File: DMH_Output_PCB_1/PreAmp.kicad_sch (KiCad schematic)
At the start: 0 parts

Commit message: Designed preamp circuit
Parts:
- added C15, C18, C20, C22: 100pF, Capacitor_THT:C_Disc_D3.0mm_W2.0mm_P2.50mm, symbol Device:C
- added C16, C17, C19, C21: 47uF, Capacitor_THT:C_Disc_D4.3mm_W1.9mm_P5.00mm, symbol Device:C
- added R60, R63, R73, R81: 100R, Resistor_THT:R_Axial_DIN0207_L6.3mm_D2.5mm_P7.62mm_Horizontal, symbol Device:R_US
- added R61, R62, R64, R65, R75, R76, R82, R83: 100k, Resistor_THT:R_Axial_DIN0207_L6.3mm_D2.5mm_P7.62mm_Horizontal, symbol Device:R_US
- added R66, R67, R68, R69, R72, R77, R78, R79: 470R, Resistor_THT:R_Axial_DIN0207_L6.3mm_D2.5mm_P7.62mm_Horizontal, symbol Device:R_US
- added R70, R71, R74, R80: 1k, Resistor_THT:R_Axial_DIN0207_L6.3mm_D2.5mm_P7.62mm_Horizontal, symbol Device:R_US
- added RV3: B10k_Dual, Potentiometer_THT:Potentiometer_Alpha_RD902F-40-00D_Dual_Vertical, symbol Device:R_Potentiometer_Dual_Separate
- added U16, U17, U18, U19: NE5532, symbol Amplifier_Operational:NE5532
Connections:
- new net: C17.2, R65.2, U16.3 (+)
- new net: C21.2, R83.2, U18.5 (+)
- new net: R66.1, U16.1, U16.2 (-)
- new net: R72.1, R74.1, R77.2, U19.2 (-)
- new net: R78.2, R79.2, R80.2, U19.3 (+)
- new net: C21.1, C22.2, R81.2, R82.2
- new net: RV3.2, U17.5 (+)
- new net: C19.1, C20.2, R73.2, R75.2
- new net: R67.1, U16.6 (-), U16.7
- new net: R67.2, R69.2, R70.2, U17.3 (+)
- new net: C15.2, C16.1, R60.2, R61.2
- new net: C17.1, C18.2, R63.2, R64.2
- new net: C19.2, R76.2, U18.3 (+)
- new net: R66.2, R68.1, R71.1, U17.2 (-)
- new net: R68.2, U17.6 (-), U17.7
- new net: C16.2, R62.2, U16.5 (+)
- new net: R77.1, U18.1, U18.2 (-)
- new net: RV3.5, U19.5 (+)
- new net: R72.2, U19.6 (-), U19.7
- new net: R78.1, U18.6 (-), U18.7
- new net GND: C15.1, C18.1, C20.1, C22.1, R61.1, R62.1, R64.1, R65.1, R69.1, R70.1, R75.1, R76.1, R79.1, R80.1, R82.1, R83.1, RV3.1, RV3.4
- new net L_Euro_OUT: R71.2, RV3.3, U17.1
- new net L_Ext_IN+: R60.1
- new net L_Ext_IN-: R63.1
- new net R_Euro_OUT: R74.2, RV3.6, U19.1
- new net R_Ext_IN+: R81.1
- new net R_Ext_IN-: R73.1

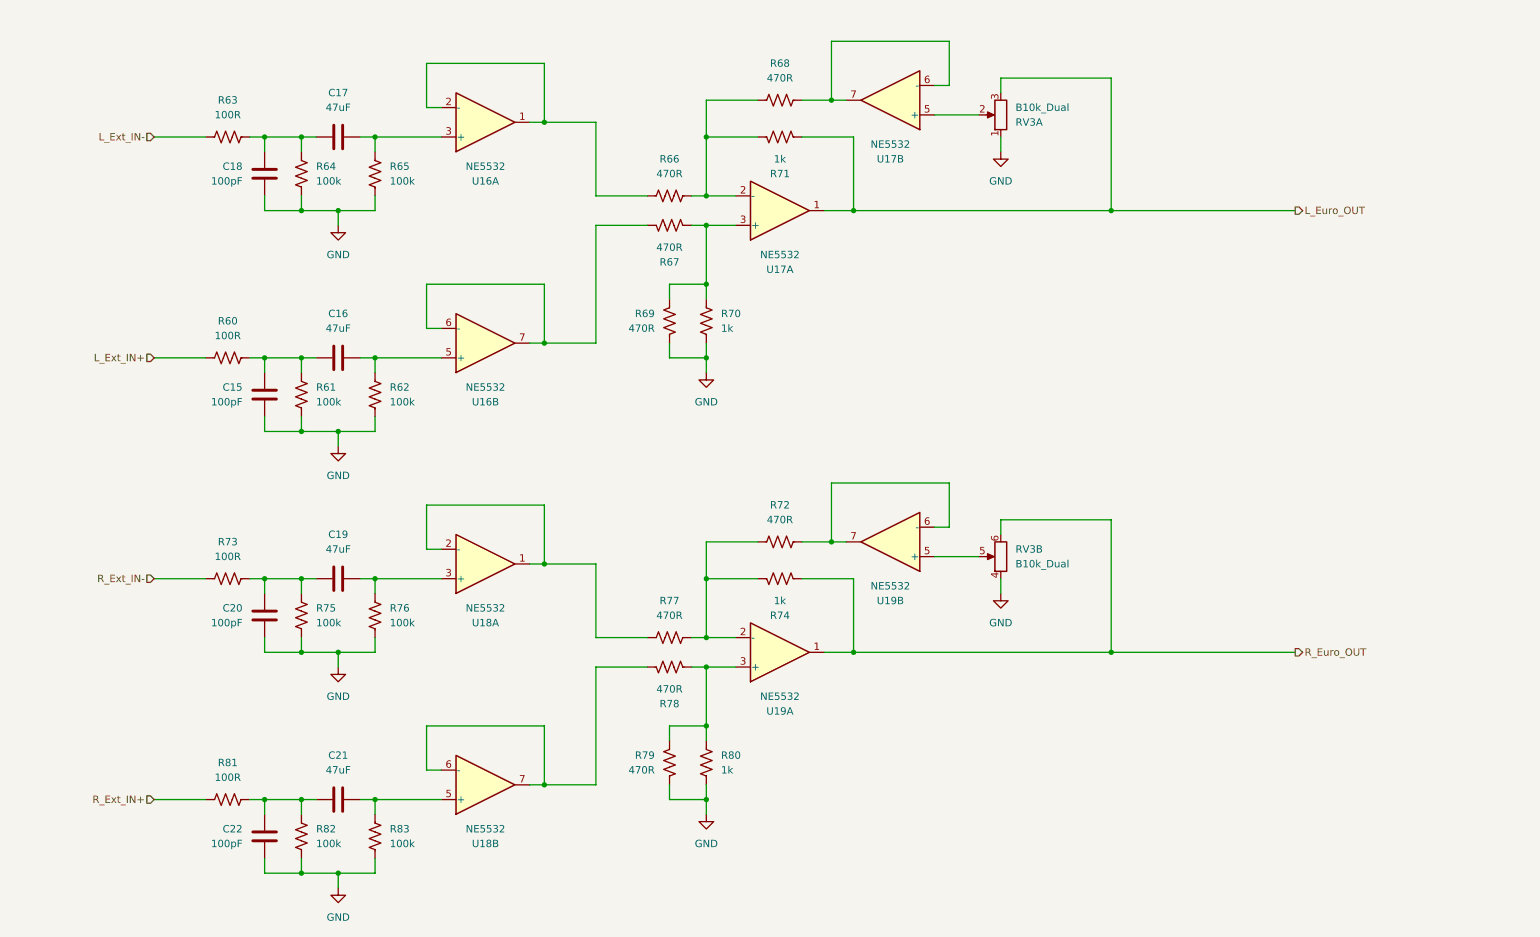
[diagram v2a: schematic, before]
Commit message: Redesigned external input preamp
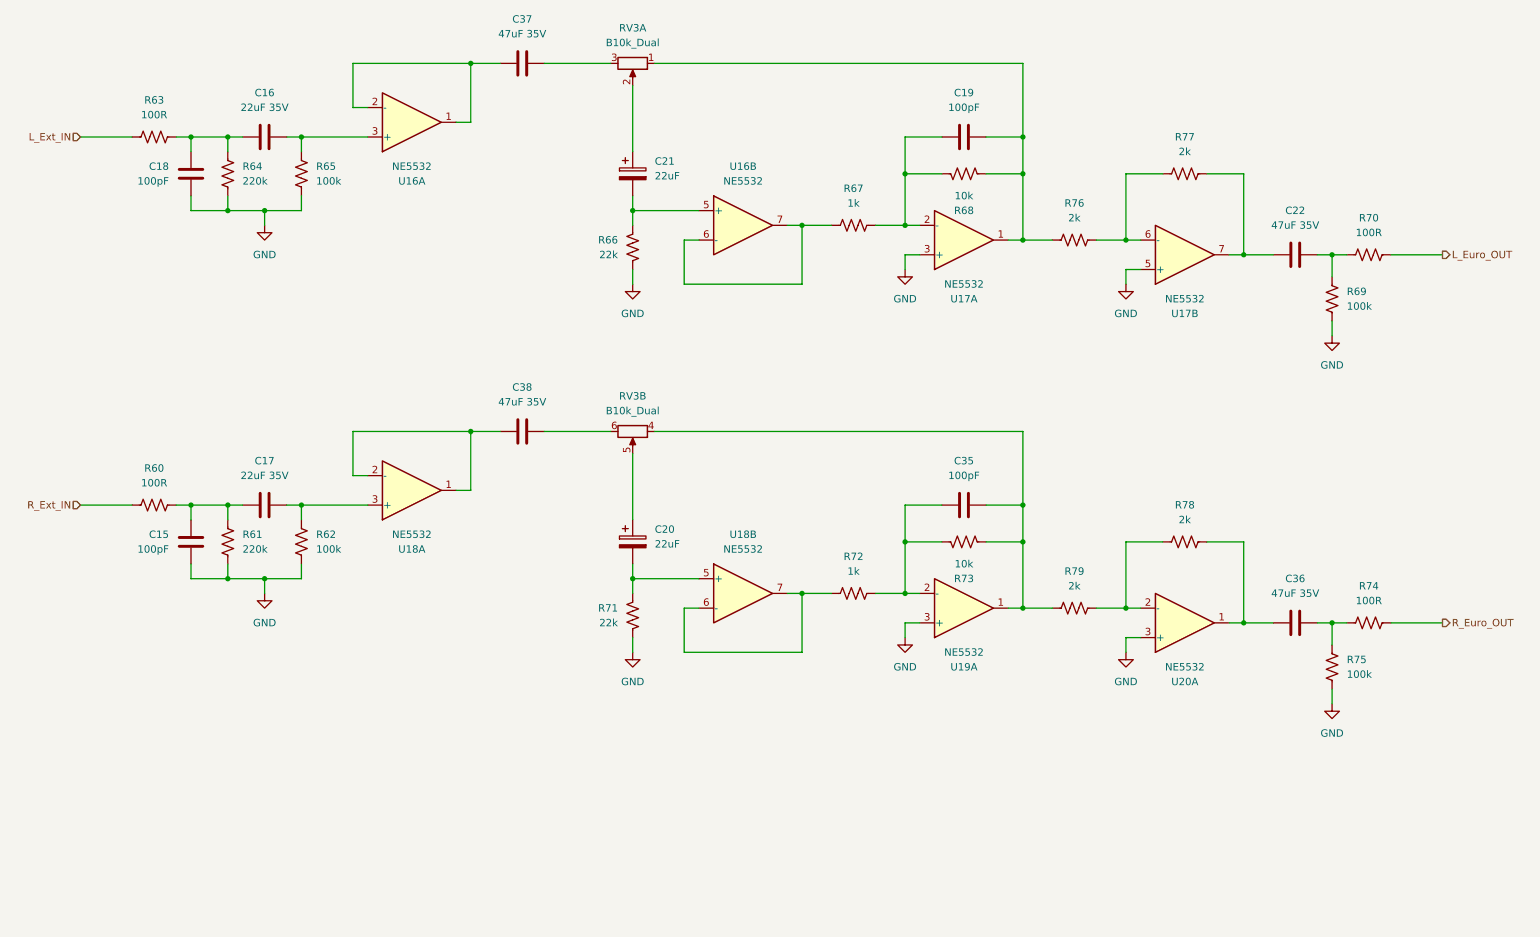
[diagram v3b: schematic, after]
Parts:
- removed C20: 100pF, Capacitor_THT:C_Disc_D3.0mm_W2.0mm_P2.50mm, symbol Device:C
- removed C21: 47uF, Capacitor_THT:C_Disc_D4.3mm_W1.9mm_P5.00mm, symbol Device:C
- removed R80: 1k, Resistor_THT:R_Axial_DIN0207_L6.3mm_D2.5mm_P7.62mm_Horizontal, symbol Device:R_US
- removed R81: 100R, Resistor_THT:R_Axial_DIN0207_L6.3mm_D2.5mm_P7.62mm_Horizontal, symbol Device:R_US
- removed R82, R83: 100k, Resistor_THT:R_Axial_DIN0207_L6.3mm_D2.5mm_P7.62mm_Horizontal, symbol Device:R_US
- removed unit 2 of U19
- added C20, C21: 22uF, Capacitor_THT:CP_Radial_D5.0mm_P2.00mm, symbol Device:C_Polarized
- added C35: 100pF, Capacitor_THT:C_Disc_D3.0mm_W2.0mm_P2.50mm, symbol Device:C
- added C36, C37, C38: 47uF 35V, Capacitor_THT:C_Radial_D8.0mm_H11.5mm_P3.50mm, symbol Device:C
- added U20: NE5532, symbol Amplifier_Operational:NE5532
- C16, C17: value 47uF -> 22uF 35V; footprint Capacitor_THT:C_Disc_D4.3mm_W1.9mm_P5.00mm -> Capacitor_THT:C_Radial_D8.0mm_H11.5mm_P3.50mm
- C19: value 47uF -> 100pF; footprint Capacitor_THT:C_Disc_D4.3mm_W1.9mm_P5.00mm -> Capacitor_THT:C_Disc_D3.0mm_W2.0mm_P2.50mm
- C22: value 100pF -> 47uF 35V; footprint Capacitor_THT:C_Disc_D3.0mm_W2.0mm_P2.50mm -> Capacitor_THT:C_Radial_D8.0mm_H11.5mm_P3.50mm
- R61, R64: value 100k -> 220k
- R66: value 470R -> 22k
- R67, R72: value 470R -> 1k
- R68: value 470R -> 10k
- R69: value 470R -> 100k
- R70, R74: value 1k -> 100R
- R71: value 1k -> 22k
- R73: value 100R -> 10k
- R76: value 100k -> 2k
- R77, R78, R79: value 470R -> 2k
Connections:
- net R_Ext_IN- is gone; now on an unnamed net: R73.1
- net GND: now also R66.1, R71.1, U17.3 (+), U17.5 (+), U19.3 (+), U20.3 (+); no longer C22.1, R70.1, R76.1, R79.1, RV3.1, RV3.4
- net L_Euro_OUT: now also R70.2; no longer R71.2, RV3.3, U17.1
- net R_Euro_OUT: no longer RV3.6, U19.1
- net at R65.2, U16.3 (+): now also C16.2; no longer C17.2
- net at U18.5 (+): now also R71.2, C20.2
- net at U16.1, U16.2 (-): now also C37.1; no longer R66.1
- net at C22.2: now also R69.2, R70.1
- net at RV3.2: now also C21.1; no longer U17.5 (+)
- net at C15.2, R60.2, R61.2: now also C17.1; no longer C16.1
- net at C18.2, R63.2, R64.2: now also C16.1; no longer C17.1
- net at R68.1, U17.2 (-): now also C19.1, R67.2; no longer R66.2, R71.1
- net at U18.1, U18.2 (-): now also C38.1; no longer R77.1
- net at RV3.5: now also C20.1
- net at R72.2: now also U19.2 (-), C35.1
- net at U18.6 (-), U18.7: now also R72.1; no longer R78.1
- net L_Ext_IN+ renamed R_Ext_IN
- net L_Ext_IN- renamed L_Ext_IN
- new net: R76.2, R77.1, U17.6 (-)
- new net: C22.1, R77.2, U17.7
- new net: R78.1, R79.2, U20.2 (-)
- new net: C36.1, R78.2, U20.1
- new net: C35.2, R73.2, R79.1, RV3.4, U19.1
- new net: C19.2, R68.2, R76.1, RV3.1, U17.1
- new net: C37.2, RV3.3
- new net: C21.2, R66.2, U16.5 (+)
- new net: C17.2, R62.2, U18.3 (+)
- new net: C38.2, RV3.6
- new net: C36.2, R74.1, R75.2
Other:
- moved on the sheet: C15, C18, R60, R61, R62, R63, R64, R65, RV3A, RV3B, U16A

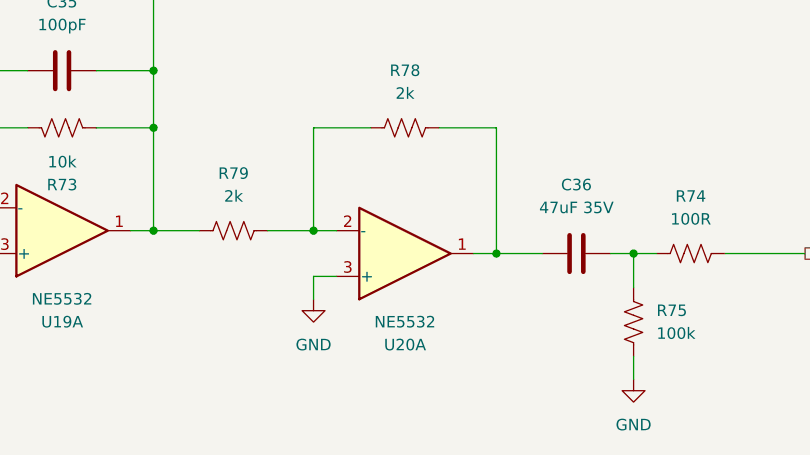
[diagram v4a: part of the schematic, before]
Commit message: Updated meters resistor values
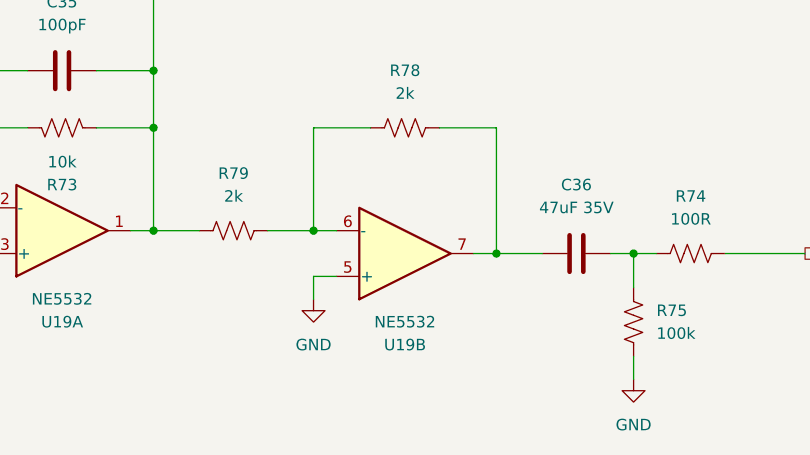
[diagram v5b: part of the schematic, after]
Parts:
- U16, U17, U18, U19: footprint (none) -> Package_DIP:DIP-8_W7.62mm_Socket
- U19: renamed from U20; footprint (none) -> Package_DIP:DIP-8_W7.62mm_Socket
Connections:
- net GND: now also U19.5 (+); no longer U19.3 (+)
- net at R78.1, R79.2: now also U19.6 (-); no longer U19.2 (-)
- net at C36.1, R78.2: now also U19.7; no longer U19.1
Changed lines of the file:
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@@
 			)
 		)
-		(property "Footprint" ""
+		(property "Footprint" "Package_DIP:DIP-8_W7.62mm_Socket"
 			(at 88.9 35.56 0)
 			(effects
@@
 			)
 		)
-		(property "Footprint" ""
+		(property "Footprint" "Package_DIP:DIP-8_W7.62mm_Socket"
 			(at 146.05 116.84 0)
 			(effects
@@
 			)
 		)
-		(property "Footprint" ""
+		(property "Footprint" "Package_DIP:DIP-8_W7.62mm_Socket"
 			(at 222.25 58.42 0)
 			(effects
@@
 			)
 		)
-		(property "Footprint" ""
+		(property "Footprint" "Package_DIP:DIP-8_W7.62mm_Socket"
 			(at 146.05 53.34 0)
 			(effects
@@
 		(at 222.25 121.92 0)
 		(mirror x)
-		(unit 1)
-		(exclude_from_sim no)
-		(in_bom yes)
-		(on_board yes)
-		(dnp no)
-		(property "Reference" "U20"
+		(unit 2)
+		(exclude_from_sim no)
+		(in_bom yes)
+		(on_board yes)
+		(dnp no)
+		(property "Reference" "U19"
 			(at 222.25 132.08 0)
 			(effects
@@
 			)
 		)
-		(property "Footprint" ""
+		(property "Footprint" "Package_DIP:DIP-8_W7.62mm_Socket"
 			(at 222.25 121.92 0)
 			(effects
@@
 			(project "DMH_Output_PCB_1"
 				(path "/58f4306d-5387-4983-bb08-41a2313fd315/2bf49d64-899a-4cd6-98ee-a1cb99869b23"
-					(reference "U20")
-					(unit 1)
+					(reference "U19")
+					(unit 2)
 				)
 			)
@@
 			)
 		)
-		(property "Footprint" ""
+		(property "Footprint" "Package_DIP:DIP-8_W7.62mm_Socket"
 			(at 184.15 55.88 0)
 			(effects
@@
 			)
 		)
-		(property "Footprint" ""
+		(property "Footprint" "Package_DIP:DIP-8_W7.62mm_Socket"
 			(at 184.15 119.38 0)
 			(effects
@@
 			)
 		)
-		(property "Footprint" ""
+		(property "Footprint" "Package_DIP:DIP-8_W7.62mm_Socket"
 			(at 88.9 99.06 0)
 			(effects
